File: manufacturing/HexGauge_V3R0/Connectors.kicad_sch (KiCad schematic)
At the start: 18 parts, among them J1 USB_B_Micro, J2 Conn_ARM_SWD_TC2030-NL, J3 Micro_SD_Card, J4 Conn_01x04_Pin, SW2 SW_Omron_B3FS, U4 USBLC6-4

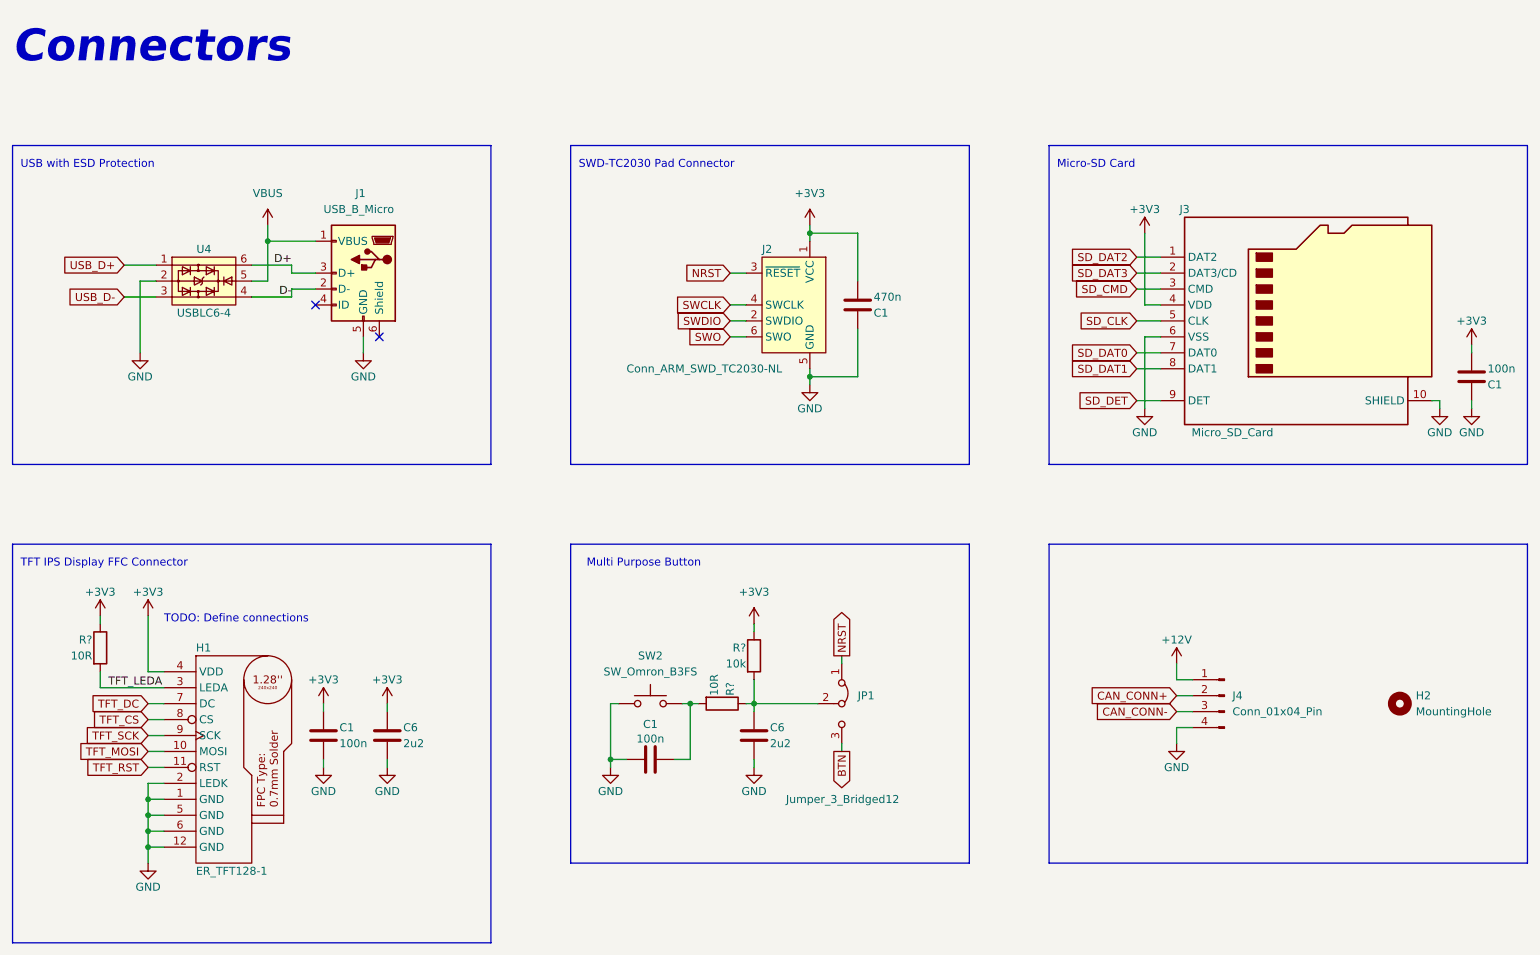
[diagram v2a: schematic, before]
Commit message: V3R0 SPI SD Card Update
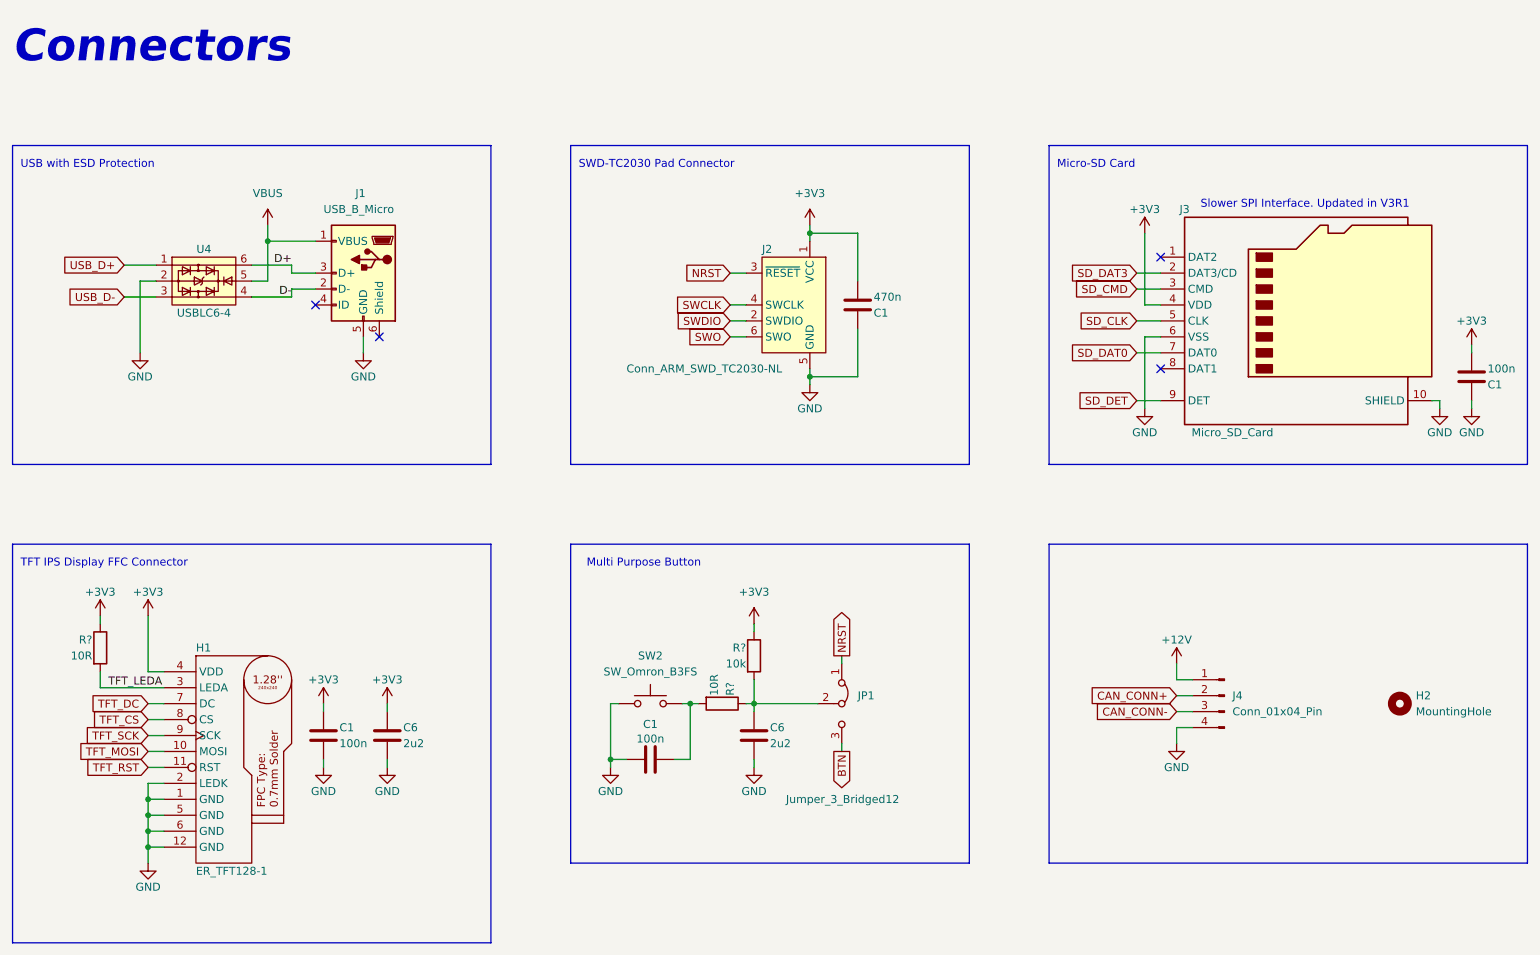
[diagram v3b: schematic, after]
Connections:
- net SD_DAT1: no longer names the net of J3.8 (DAT1)
- net SD_DAT2: no longer names the net of J3.1 (DAT2)
- no-connect marks 2 -> 4
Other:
- note added: "Slower SPI Interface. Updated in V3R1"
- note removed: "TODO: Define connections"
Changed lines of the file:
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@@
   (junction (at 120.65 135.89) (diameter 0) (color 0 0 0 0)
   )
+  (no_connect (at 208.28 55.88))
   (no_connect (at 73.66 63.5))
+  (no_connect (at 208.28 73.66))
   (no_connect (at 83.82 68.58))
   (wire (pts (xy 46.99 139.7) (xy 46.99 142.24))
@@
     (stroke (width 0) (type default))
   )
-  (wire (pts (xy 204.47 55.88) (xy 208.28 55.88))
-    (stroke (width 0) (type default))
-  )
   (wire (pts (xy 210.82 120.65) (xy 210.82 123.19))
     (stroke (width 0) (type default))
@@
     (stroke (width 0) (type default))
   )
-  (wire (pts (xy 204.47 73.66) (xy 208.28 73.66))
-    (stroke (width 0) (type default))
-  )
   (wire (pts (xy 46.99 144.78) (xy 46.99 147.32))
     (stroke (width 0) (type default))
@@
     (effects (font (size 1.27 1.27)) (justify left bottom))
   )
+  (text "Slower SPI Interface. Updated in V3R1" (at 214.63 48.26 0)
+    (effects (font (size 1.27 1.27)) (justify left bottom))
+  )
   (text "SWD-TC2030 Pad Connector\n" (at 115.57 41.91 0)
     (effects (font (size 1.27 1.27)) (justify left bottom))
   )
   (text "Micro-SD Card\n" (at 191.77 41.91 0)
-    (effects (font (size 1.27 1.27)) (justify left bottom))
-  )
-  (text "TODO: Define connections" (at 49.53 114.3 0)
     (effects (font (size 1.27 1.27)) (justify left bottom))
   )
@@
     (effects (font (size 1.27 1.27)) (justify right))
     (property "Intersheetrefs" "${INTERSHEET_REFS}" (at 194.7305 78.74 0)
-      (effects (font (size 1.27 1.27)) (justify right) hide)
-    )
-  )
-  (global_label "SD_DAT2" (shape input) (at 204.47 55.88 180) (fields_autoplaced)
-    (effects (font (size 1.27 1.27)) (justify right))
-    (property "Intersheetrefs" "${INTERSHEET_REFS}" (at 193.5814 55.88 0)
       (effects (font (size 1.27 1.27)) (justify right) hide)
     )
@@
       (effects (font (size 1.27 1.27)) (justify right) hide)
     )
-  )
-  (global_label "SD_DAT1" (shape input) (at 204.47 73.66 180) (fields_autoplaced)
-    (effects (font (size 1.27 1.27)) (justify right))
-    (property "Intersheetrefs" "${INTERSHEET_REFS}" (at 193.5814 73.66 0)
-      (effects (font (size 1.27 1.27)) (justify right) hide)
-    )
